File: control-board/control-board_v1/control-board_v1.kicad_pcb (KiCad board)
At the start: 4 copper layers, 68.6 x 53.3 mm, 77 parts, among them J1 Barrel_Jack, J2 Header-M_2x6, J3 Header-M_2x6, J4 Header-M_2x6, J5 Header-M_2x6, J6 Header_1x8, J7 Header_1x8, J8 Header_1x10, J9 Header_1x8, Q1 PMOS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

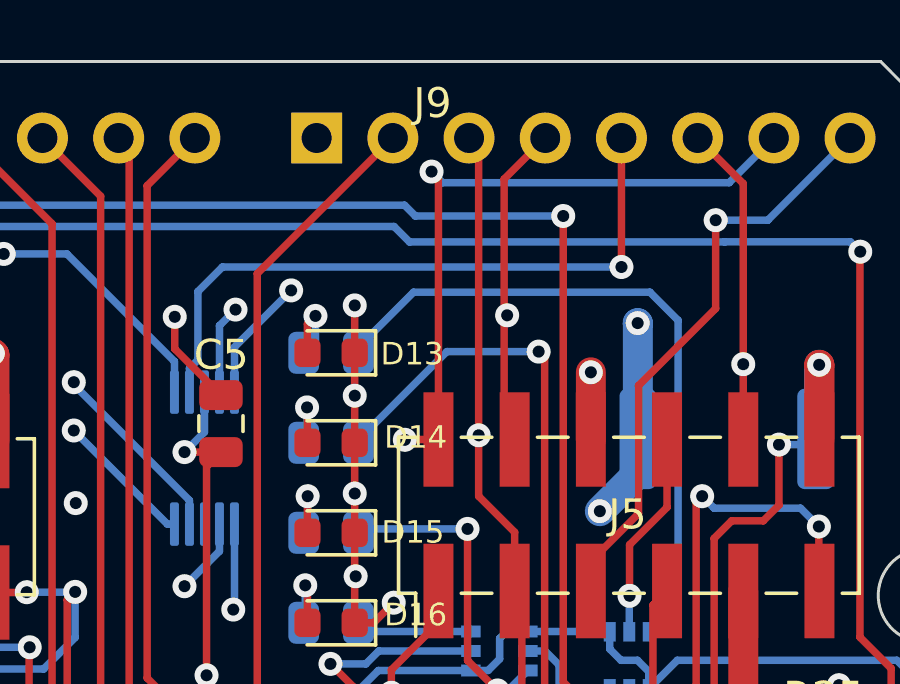
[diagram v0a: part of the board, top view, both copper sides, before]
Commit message: pulldown resistor
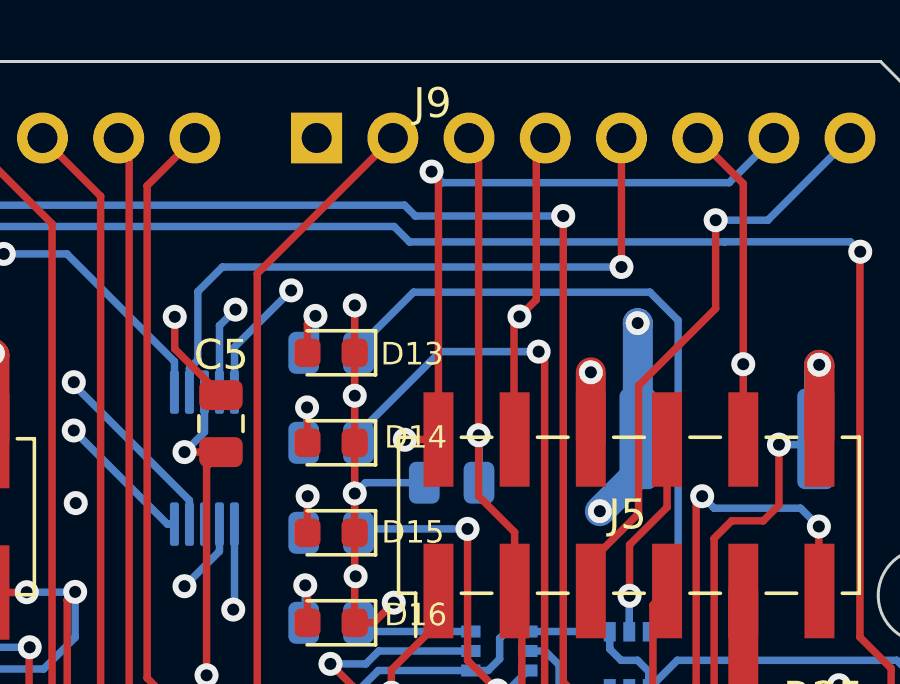
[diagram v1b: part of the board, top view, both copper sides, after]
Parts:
- added R29: 10K, Resistor_SMD:R_0805_2012Metric, B.Cu at (67.1, 29.3)
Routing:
- net GND: track 123.8 -> 126.2 mm
- net ~{RDY}: track 110.0 -> 111.5 mm

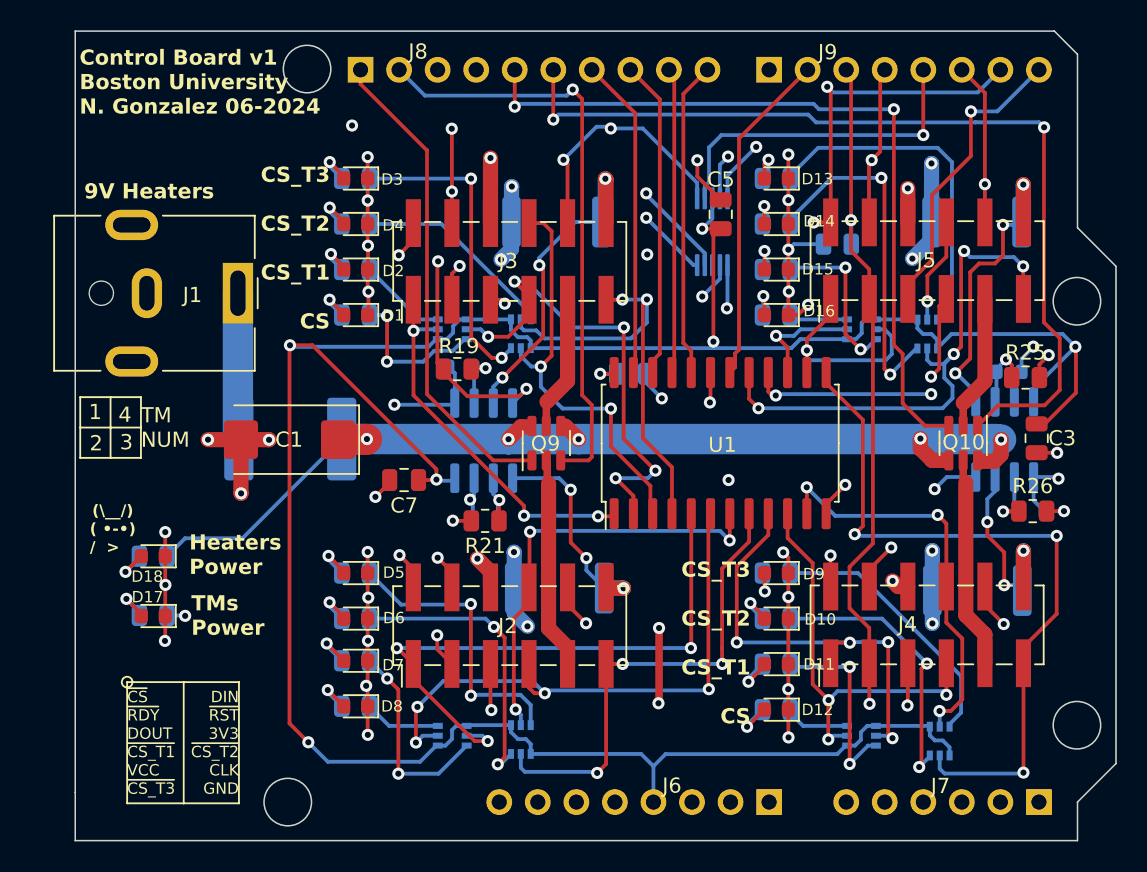
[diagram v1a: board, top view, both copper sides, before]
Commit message: fixed RDYB logic in pcb
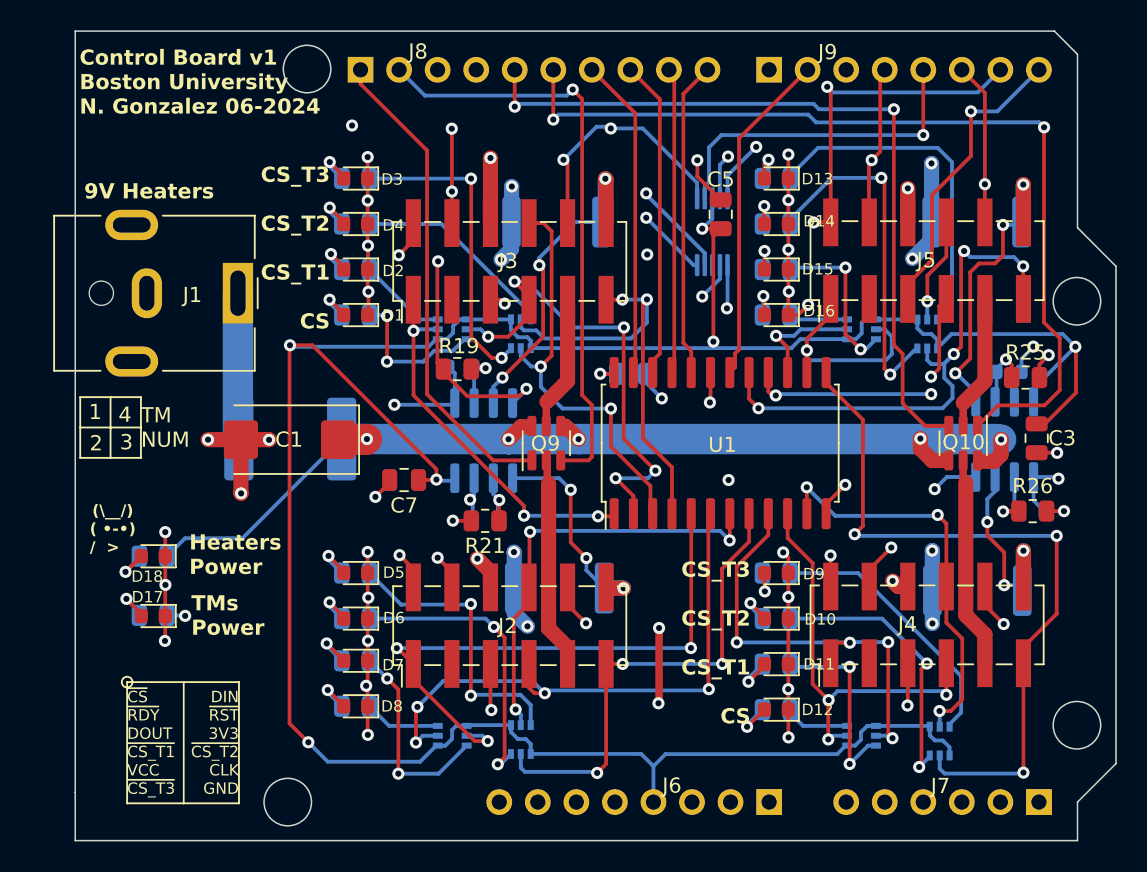
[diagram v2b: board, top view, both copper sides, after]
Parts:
- removed R29: 10K, Resistor_SMD:R_0805_2012Metric
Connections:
- J2 pad 3: ~{RDY} -> unconnected-(J2-Pin_3-Pad3)
- J3 pad 3: ~{RDY} -> unconnected-(J3-Pin_3-Pad3)
- J4 pad 3: ~{RDY} -> unconnected-(J4-Pin_3-Pad3)
- J5 pad 3: ~{RDY} -> unconnected-(J5-Pin_3-Pad3)
- J9 pad 3: ~{RDY} -> unconnected-(J9-Pin_3-Pad3)
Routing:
- net ~{RDY}: track 111.5 -> 0.00 mm, vias 4 -> 0
- net GND: track 126.2 -> 123.8 mm
